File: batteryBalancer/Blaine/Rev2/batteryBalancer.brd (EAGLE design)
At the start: 101.6 x 101.6 mm, 53 parts

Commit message: Last commit of Battery balancer Rev 1
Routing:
- net KILL_SWITCH: track 211.4 -> 212.2 mm
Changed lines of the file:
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@@
 <wire x1="26.5" y1="3.175" x2="26.6855" y2="3.175" width="0.1524" layer="1"/>
 <contactref element="RLAY1" pad="CONTROL-"/>
-<contactref element="RELAY4" pad="CONTROL-"/>
 <contactref element="RELAY3" pad="CONTROL-"/>
 <contactref element="RELAY2" pad="CONTROL-"/>
@@
 <wire x1="74.2875" y1="36.8375" x2="73.66" y2="37.465" width="0.1524" layer="16"/>
 <wire x1="65.5" y1="99" x2="66.5" y2="99" width="0.1524" layer="1"/>
-<wire x1="27.432" y1="17.955" x2="25.75" y2="17.955" width="1.016" layer="1"/>
 <wire x1="27.432" y1="17.955" x2="35.9875" y2="17.955" width="1.016" layer="1"/>
 <wire x1="35.9875" y1="17.955" x2="36" y2="17.9675" width="1.016" layer="1"/>
@@
 <wire x1="69.088" y1="39.624" x2="69.85" y2="40.386" width="0.1524" layer="1"/>
 <wire x1="69.85" y1="40.386" x2="73.66" y2="40.386" width="0.1524" layer="1"/>
+<contactref element="RELAY4" pad="CONTROL-"/>
+<wire x1="25.75" y1="17.955" x2="27.432" y2="17.955" width="1.016" layer="1"/>
+<wire x1="26.6855" y1="8" x2="27.75" y2="8.25" width="0" layer="19" extent="16-16"/>
+<wire x1="26.6855" y1="7.1855" x2="26.6855" y2="8" width="0" layer="19" extent="16-16"/>
+<wire x1="26.6855" y1="3.175" x2="26.6855" y2="3.175" width="0" layer="19" extent="1-16"/>
+<wire x1="24.1455" y1="3.175" x2="26.5" y2="3.175" width="0" layer="19" extent="1-16"/>
+<wire x1="24.1455" y1="3.175" x2="24.1455" y2="3.175" width="0" layer="19" extent="1-16"/>
+<wire x1="29.2255" y1="3.175" x2="26.6855" y2="3.175" width="0" layer="19" extent="16-16"/>
+<wire x1="29.2255" y1="3.175" x2="29.2255" y2="3.175" width="0" layer="19" extent="1-16"/>
 </signal>
 <signal name="PORT_UNBALANCED">
@@
 <wire x1="91.2148" y1="11.9539125" x2="91.2148" y2="88.5352" width="0.1524" layer="1"/>
 <wire x1="25.75" y1="23.055" x2="18.2282" y2="23.055" width="1.016" layer="1"/>
-<wire x1="18.2282" y1="23.055" x2="14.1732" y2="19" width="1.016" layer="1"/>
+<wire x1="14.1732" y1="19" x2="18.2282" y2="23.055" width="1.016" layer="1"/>
 <contactref element="KILL_SWITCH" pad="1"/>
-<wire x1="14.1732" y1="18.161" x2="14.1732" y2="19" width="0" layer="19" extent="1-1"/>
+<wire x1="14.1732" y1="18.161" x2="14.1732" y2="19" width="1.016" layer="1"/>
 </signal>
 <signal name="STBD_UNFUSED">

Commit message: Touched up the battery balancer
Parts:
- removed C3, C4, C5, C6: 0.1uF, SparkFun-Capacitors:CAP-PTH-SMALL-KIT
- moved C2 20.3 mm to (65.9, 22.2), turned to 90 degrees
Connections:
- net 3.3V: now also C2.2
- net BALANCED_LOGIC: no longer C3.1
- net LOGIC_GND: now also C2.1; no longer C2.2, C3.2, C4.2, C5.2, C6.2
- net PORT_CURRENT: no longer C4.1
- net PORT_LOGIC: no longer C6.1
- net STBD_CURRENT: no longer C2.1
- net STBD_LOGIC: no longer C5.1
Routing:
- net LOGIC_GND: track 404.0 -> 386.7 mm
- net PORT_CURRENT: track 78.7 -> 68.9 mm
- net STBD_CURRENT: track 145.3 -> 139.9 mm
- net PORT_LOGIC: track 61.6 -> 56.2 mm
- net BALANCED_LOGIC: track 111.5 -> 108.2 mm
- net STBD_LOGIC: track 129.6 -> 127.2 mm
- net 3.3V: track 290.9 -> 293.2 mm
- net SDA: track 32.1 -> 33.5 mm
- net SCL: track 33.3 -> 34.6 mm
- net MOTOR_POWER1: track 57.0 -> 55.9 mm

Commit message: Fixed optoisolator values
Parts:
- R10, R11, R9: value 470 -> 10K
- R12, R13, R14: value 100 -> 2.2K
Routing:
- net GND: track 39.9 -> 32.5 mm
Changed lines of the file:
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@@
 <attribute name="OC_NEWARK" value="21H7744" x="10.541" y="56.515" size="1.778" layer="27" rot="R90" display="off"/>
 </element>
-<element name="R9" library="rcl" library_urn="urn:adsk.eagle:library:334" package="0207/7" package3d_urn="urn:adsk.eagle:package:23493/1" value="470" x="17.526" y="66.548" rot="R90"/>
-<element name="R10" library="rcl" library_urn="urn:adsk.eagle:library:334" package="0207/7" package3d_urn="urn:adsk.eagle:package:23493/1" value="470" x="75.692" y="48.514" rot="R180"/>
-<element name="R11" library="rcl" library_urn="urn:adsk.eagle:library:334" package="0207/7" package3d_urn="urn:adsk.eagle:package:23493/1" value="470" x="20.574" y="53.975" rot="R270"/>
-<element name="R12" library="rcl" library_urn="urn:adsk.eagle:library:334" package="0207/7" package3d_urn="urn:adsk.eagle:package:23493/1" value="100" x="3.048" y="64.77" rot="R90"/>
-<element name="R13" library="rcl" library_urn="urn:adsk.eagle:library:334" package="0207/7" package3d_urn="urn:adsk.eagle:package:23493/1" value="100" x="97.282" y="50.927" rot="R270"/>
-<element name="R14" library="rcl" library_urn="urn:adsk.eagle:library:334" package="0207/7" package3d_urn="urn:adsk.eagle:package:23493/1" value="100" x="3.048" y="54.61" rot="R270"/>
+<element name="R9" library="rcl" library_urn="urn:adsk.eagle:library:334" package="0207/7" package3d_urn="urn:adsk.eagle:package:23493/1" value="10K" x="17.526" y="66.548" rot="R90"/>
+<element name="R10" library="rcl" library_urn="urn:adsk.eagle:library:334" package="0207/7" package3d_urn="urn:adsk.eagle:package:23493/1" value="10K" x="75.692" y="48.514" rot="R180"/>
+<element name="R11" library="rcl" library_urn="urn:adsk.eagle:library:334" package="0207/7" package3d_urn="urn:adsk.eagle:package:23493/1" value="10K" x="20.574" y="53.975" rot="R270"/>
+<element name="R12" library="rcl" library_urn="urn:adsk.eagle:library:334" package="0207/7" package3d_urn="urn:adsk.eagle:package:23493/1" value="2.2K" x="3.048" y="64.77" rot="R90"/>
+<element name="R13" library="rcl" library_urn="urn:adsk.eagle:library:334" package="0207/7" package3d_urn="urn:adsk.eagle:package:23493/1" value="2.2K" x="97.282" y="50.927" rot="R270"/>
+<element name="R14" library="rcl" library_urn="urn:adsk.eagle:library:334" package="0207/7" package3d_urn="urn:adsk.eagle:package:23493/1" value="2.2K" x="3.048" y="54.61" rot="R270"/>
 <element name="R15" library="rcl" library_urn="urn:adsk.eagle:library:334" package="0207/7" package3d_urn="urn:adsk.eagle:package:23493/1" value="4.7K" x="20.828" y="66.548" rot="R90"/>
 <element name="R16" library="rcl" library_urn="urn:adsk.eagle:library:334" package="0207/7" package3d_urn="urn:adsk.eagle:package:23493/1" value="4.7K" x="75.692" y="51.308" rot="R180"/>
@@
 <contactref element="R11" pad="2"/>
 <contactref element="PORT_FC" pad="2"/>
-<wire x1="64.12223125" y1="85.852" x2="63.05363125" y2="86.9206" width="0.4064" layer="16"/>
-<wire x1="63.05363125" y1="86.9206" x2="62.0286" y2="86.9206" width="0.4064" layer="16"/>
-<wire x1="62.0286" y1="86.9206" x2="58.547" y2="83.439" width="0.4064" layer="16"/>
 <via x="58.547" y="83.439" extent="1-16" drill="0.35"/>
 <wire x1="58.547" y1="83.439" x2="58.547" y2="82.169" width="0.4064" layer="1"/>

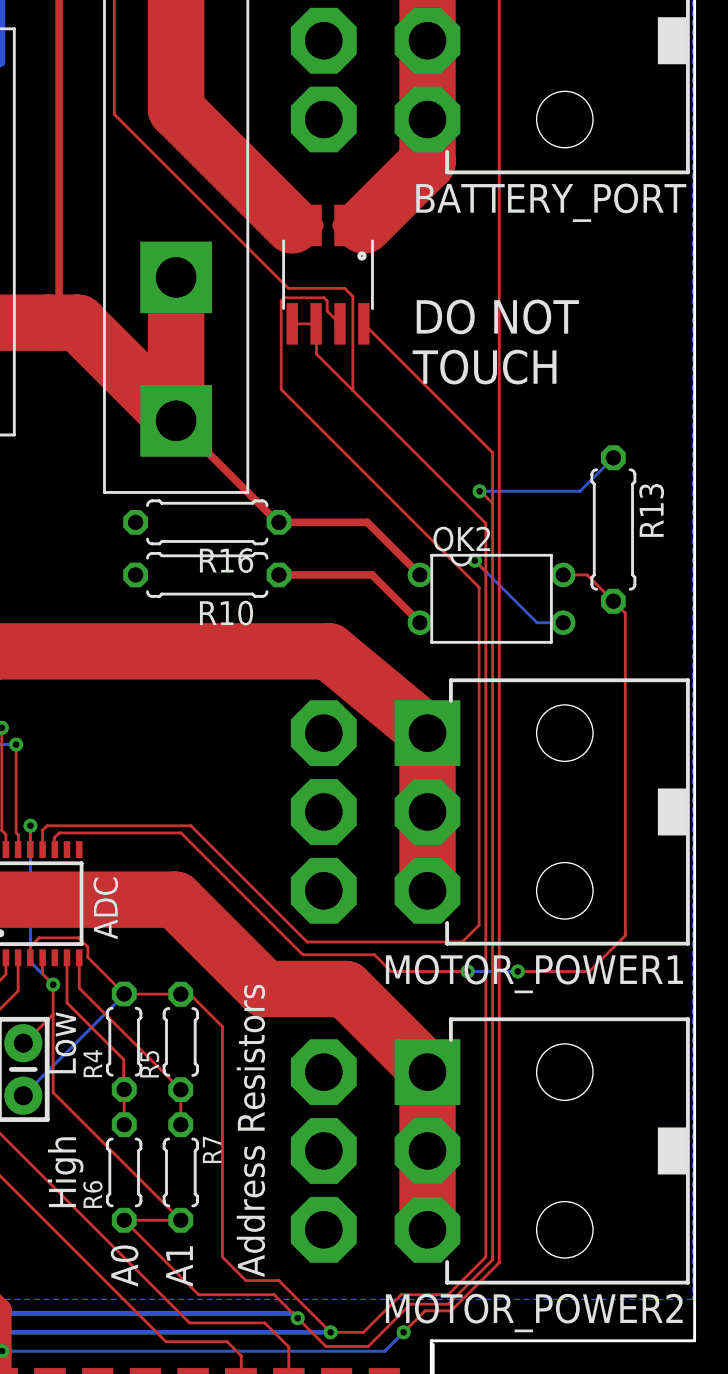
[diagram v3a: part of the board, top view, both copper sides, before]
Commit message: Updated board and added block diagram
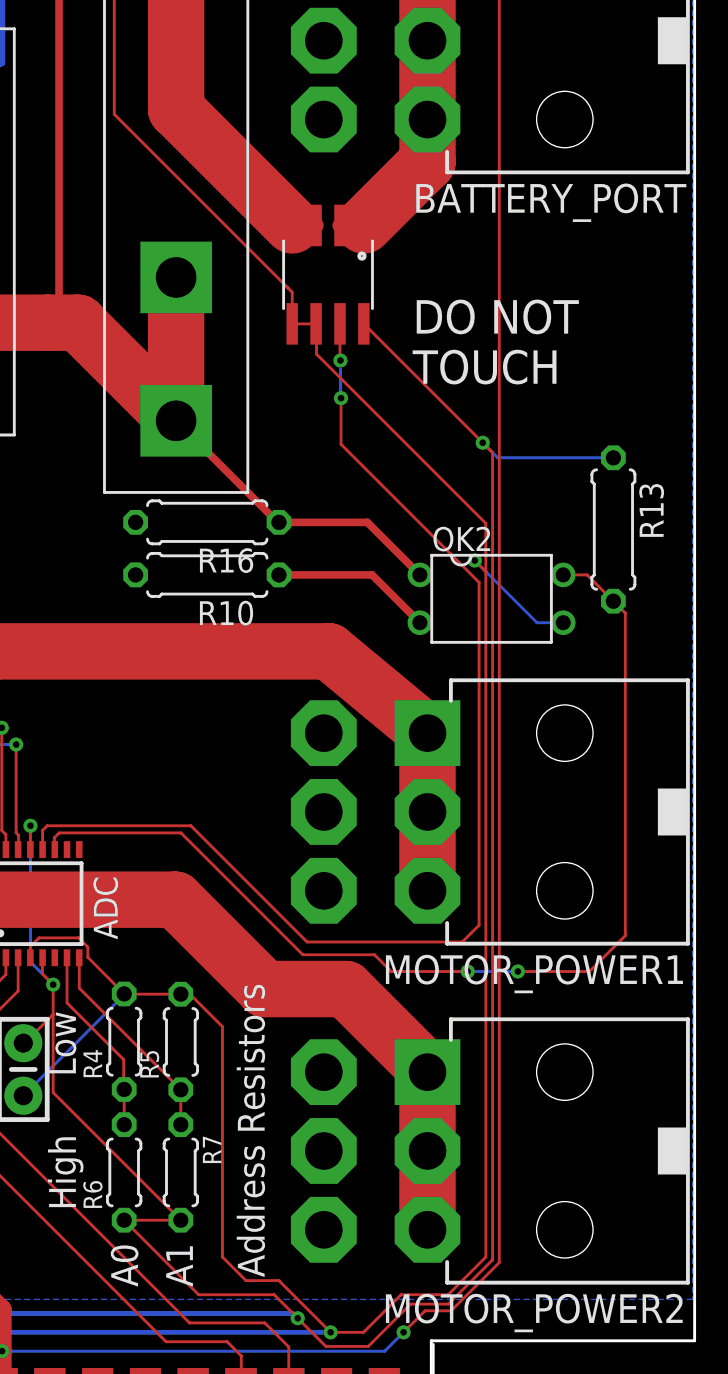
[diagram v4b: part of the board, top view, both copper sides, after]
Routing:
- net PORT_CURRENT: track 68.9 -> 62.3 mm, vias 0 -> 2
- net LOGIC_GND: track 386.7 -> 380.2 mm
- net 3.3V: track 293.2 -> 291.6 mm
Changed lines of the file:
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@@
 <layer number="27" name="tValues" color="7" fill="1" visible="yes" active="yes"/>
 <layer number="28" name="bValues" color="7" fill="1" visible="yes" active="yes"/>
-<layer number="29" name="tStop" color="7" fill="3" visible="no" active="yes"/>
-<layer number="30" name="bStop" color="7" fill="6" visible="no" active="yes"/>
-<layer number="31" name="tCream" color="7" fill="4" visible="no" active="yes"/>
-<layer number="32" name="bCream" color="7" fill="5" visible="no" active="yes"/>
-<layer number="33" name="tFinish" color="6" fill="3" visible="no" active="yes"/>
-<layer number="34" name="bFinish" color="6" fill="6" visible="no" active="yes"/>
-<layer number="35" name="tGlue" color="7" fill="4" visible="no" active="yes"/>
-<layer number="36" name="bGlue" color="7" fill="5" visible="no" active="yes"/>
-<layer number="37" name="tTest" color="7" fill="1" visible="no" active="yes"/>
-<layer number="38" name="bTest" color="7" fill="1" visible="no" active="yes"/>
+<layer number="29" name="tStop" color="7" fill="3" visible="yes" active="yes"/>
+<layer number="30" name="bStop" color="7" fill="6" visible="yes" active="yes"/>
+<layer number="31" name="tCream" color="7" fill="4" visible="yes" active="yes"/>
+<layer number="32" name="bCream" color="7" fill="5" visible="yes" active="yes"/>
+<layer number="33" name="tFinish" color="6" fill="3" visible="yes" active="yes"/>
+<layer number="34" name="bFinish" color="6" fill="6" visible="yes" active="yes"/>
+<layer number="35" name="tGlue" color="7" fill="4" visible="yes" active="yes"/>
+<layer number="36" name="bGlue" color="7" fill="5" visible="yes" active="yes"/>
+<layer number="37" name="tTest" color="7" fill="1" visible="yes" active="yes"/>
+<layer number="38" name="bTest" color="7" fill="1" visible="yes" active="yes"/>
 <layer number="39" name="tKeepout" color="4" fill="11" visible="yes" active="yes"/>
 <layer number="40" name="bKeepout" color="1" fill="11" visible="yes" active="yes"/>
@@
 <layer number="42" name="bRestrict" color="1" fill="10" visible="yes" active="yes"/>
 <layer number="43" name="vRestrict" color="2" fill="10" visible="yes" active="yes"/>
-<layer number="44" name="Drills" color="7" fill="1" visible="no" active="yes"/>
+<layer number="44" name="Drills" color="7" fill="1" visible="yes" active="yes"/>
 <layer number="45" name="Holes" color="7" fill="1" visible="yes" active="yes"/>
-<layer number="46" name="Milling" color="3" fill="1" visible="no" active="yes"/>
-<layer number="47" name="Measures" color="7" fill="1" visible="no" active="yes"/>
+<layer number="46" name="Milling" color="3" fill="1" visible="yes" active="yes"/>
+<layer number="47" name="Measures" color="7" fill="1" visible="yes" active="yes"/>
 <layer number="48" name="Document" color="7" fill="1" visible="yes" active="yes"/>
 <layer number="49" name="Reference" color="7" fill="1" visible="yes" active="yes"/>
@@
 <layer number="112" name="tSilk" color="7" fill="1" visible="yes" active="yes"/>
 <layer number="113" name="IDFDebug" color="7" fill="1" visible="yes" active="yes"/>
-<layer number="114" name="Badge_Outline" color="7" fill="1" visible="no" active="yes"/>
-<layer number="115" name="ReferenceISLANDS" color="7" fill="1" visible="no" active="yes"/>
+<layer number="114" name="Badge_Outline" color="7" fill="1" visible="yes" active="yes"/>
+<layer number="115" name="ReferenceISLANDS" color="7" fill="1" visible="yes" active="yes"/>
 <layer number="116" name="Patch_BOT" color="9" fill="4" visible="yes" active="yes"/>
 <layer number="118" name="Rect_Pads" color="7" fill="1" visible="no" active="no"/>
@@
 <wire x1="76.5" y1="24.5" x2="76.5" y2="12.25" width="0.1524" layer="1"/>
 <wire x1="76.5" y1="12.25" x2="77.75" y2="11" width="0.1524" layer="1"/>
-<wire x1="83.4315" y1="58.3185" x2="90.5" y2="51.25" width="0.1524" layer="1"/>
-<wire x1="81.5" y1="60.25" x2="83.4315" y2="58.3185" width="0.1524" layer="1"/>
+<wire x1="81.5" y1="60.25" x2="90.5" y2="51.25" width="0.1524" layer="1"/>
 <wire x1="90.5" y1="12.25" x2="90.5" y2="48.692" width="0.1524" layer="1"/>
 <wire x1="90.5" y1="48.692" x2="90.5" y2="51.25" width="0.1524" layer="1"/>
@@
 <via x="82.25" y="8.25" extent="1-16" drill="0.35"/>
 <wire x1="27.75" y1="8.25" x2="82.25" y2="8.25" width="0.254" layer="16"/>
-<wire x1="83" y1="63.75" x2="83.4315" y2="63.3185" width="0.1524" layer="1"/>
-<wire x1="83" y1="63.75" x2="80" y2="63.75" width="0.1524" layer="1"/>
 <wire x1="70.75" y1="73" x2="70.75" y2="90.75" width="0.1524" layer="1"/>
 <wire x1="70.75" y1="90.75" x2="70.25" y2="91.25" width="0.1524" layer="1"/>
 <via x="70.25" y="91.25" extent="1-16" drill="0.35"/>
 <wire x1="65.5" y1="96" x2="64.5" y2="96.75" width="0.1524" layer="16"/>
-<wire x1="80" y1="63.75" x2="70.75" y2="73" width="0.1524" layer="1"/>
+<wire x1="80" y1="63.75" x2="79.9395" y2="63.8105" width="0.1524" layer="1"/>
+<wire x1="79.9395" y1="63.8105" x2="70.75" y2="73" width="0.1524" layer="1"/>
 <wire x1="70.25" y1="91.25" x2="65.5" y2="96" width="0.1524" layer="16"/>
 <via x="64.5" y="96.75" extent="1-16" drill="0.35"/>
 <wire x1="64.5" y1="98" x2="65.5" y2="99" width="0.1524" layer="1"/>
 <wire x1="64.5" y1="98" x2="64.5" y2="96.75" width="0.1524" layer="1"/>
-<wire x1="83.4315" y1="63.3185" x2="83.4315" y2="58.3185" width="0.1524" layer="1"/>
 <contactref element="KILL_STATUS" pad="CATHODE"/>
 <contactref element="STBD_CS" pad="GND"/>
@@
 <wire x1="65.913" y1="20.828" x2="71.275" y2="26.19" width="0.1524" layer="16"/>
 <wire x1="71.275" y1="26.19" x2="71.275" y2="26.24" width="0.1524" layer="16"/>
+<wire x1="79.9395" y1="63.8105" x2="80.2075" y2="63.5425" width="0.1524" layer="1"/>
+<wire x1="80.2075" y1="63.5425" x2="80.2075" y2="61.8588" width="0.1524" layer="1"/>
 </signal>
 <signal name="PORT_UNBALANCED">
@@
 <contactref element="R6" pad="1"/>
 <contactref element="R7" pad="2"/>
-<wire x1="90.8574" y1="12.10195625" x2="90.8574" y2="52.324" width="0.1524" layer="1"/>
-<wire x1="90.8574" y1="52.324" x2="90.8574" y2="55.0189" width="0.1524" layer="1"/>
+<wire x1="90.8574" y1="12.10195625" x2="90.8574" y2="55.0189" width="0.1524" layer="1"/>
 <wire x1="79.25" y1="10.25" x2="80.5" y2="9" width="0.1524" layer="1"/>
 <wire x1="80.5" y1="9" x2="82" y2="7.5" width="0.1524" layer="1"/>
@@
 <contactref element="R12" pad="1"/>
 <contactref element="KILL_SWITCH" pad="2"/>
-<wire x1="90.8574" y1="55.0189" x2="84.0175" y2="61.8588" width="0.1524" layer="1"/>
+<wire x1="90.8574" y1="55.0189" x2="90.33715" y2="55.53915" width="0.1524" layer="1"/>
+<wire x1="90.33715" y1="55.53915" x2="84.0175" y2="61.8588" width="0.1524" layer="1"/>
 <wire x1="19.685" y1="18.161" x2="19.685" y2="9.25" width="0.4064" layer="16"/>
 <wire x1="10.25" y1="86.7087" x2="16.77" y2="93.2287" width="0.1524" layer="1"/>
@@
 <wire x1="3.048" y1="58.42" x2="6.731" y2="62.103" width="0.1524" layer="1"/>
 <wire x1="6.731" y1="62.103" x2="10.25" y2="62.103" width="0.1524" layer="1"/>
-<wire x1="90.8574" y1="52.324" x2="90.2224" y2="52.959" width="0.1524" layer="1"/>
-<wire x1="90.2224" y1="52.959" x2="90.17" y2="52.959" width="0.1524" layer="1"/>
-<via x="90.17" y="52.959" extent="1-16" drill="0.35"/>
-<wire x1="90.17" y1="52.959" x2="95.504" y2="52.959" width="0.1524" layer="16"/>
-<wire x1="95.504" y1="52.959" x2="97.282" y2="54.737" width="0.1524" layer="16"/>
 <contactref element="ADC" pad="IN3"/>
 <wire x1="66.2875" y1="33.9125" x2="66.2875" y2="35.1725" width="0.1524" layer="1"/>
@@
 <wire x1="65.913" y1="23.622" x2="65.976" y2="23.622" width="0.1524" layer="1"/>
 <wire x1="65.976" y1="23.622" x2="67.5" y2="25.146" width="0.1524" layer="1"/>
+<wire x1="97.282" y1="54.737" x2="91.1393" y2="54.737" width="0.1524" layer="16"/>
+<wire x1="91.1393" y1="54.737" x2="90.33715" y2="55.53915" width="0.1524" layer="16"/>
+<via x="90.33715" y="55.53915" extent="1-16" drill="0.35"/>
 </signal>
 <signal name="ADC_A0">
@@
 <signal name="PORT_CURRENT">
 <contactref element="PORT_CS" pad="VIOUT"/>
-<wire x1="82.0635" y1="63.080175" x2="81.898775" y2="63.2449" width="0.1524" layer="1"/>
-<wire x1="79.786225" y1="63.2449" x2="79.6215" y2="63.080175" width="0.1524" layer="1"/>
-<wire x1="81.898775" y1="63.2449" x2="79.786225" y2="63.2449" width="0.1524" layer="1"/>
-<wire x1="82.7475" y1="61.8588" x2="82.0635" y2="62.5428" width="0.1524" layer="1"/>
-<wire x1="82.0635" y1="62.5428" x2="82.0635" y2="63.080175" width="0.1524" layer="1"/>
-<wire x1="79.6215" y1="63.080175" x2="79.6215" y2="58.3785" width="0.1524" layer="1"/>
-<wire x1="79.6215" y1="58.3785" x2="90.1426" y2="47.8574" width="0.1524" layer="1"/>
-<wire x1="90.1426" y1="47.8574" x2="90.1426" y2="29.8926" width="0.1524" layer="1"/>
+<wire x1="90.1426" y1="48.1168625" x2="90.1426" y2="29.8926" width="0.1524" layer="1"/>
 <wire x1="90.1426" y1="29.8926" x2="89.25" y2="29" width="0.1524" layer="1"/>
 <wire x1="81" y1="29" x2="89.25" y2="29" width="0.1524" layer="1"/>
@@
 <wire x1="67.183" y1="35.179" x2="74.821" y2="35.179" width="0.1524" layer="1"/>
 <wire x1="74.821" y1="35.179" x2="81" y2="29" width="0.1524" layer="1"/>
+<via x="82.7721" y="59.9104375" extent="1-16" drill="0.35"/>
+<wire x1="82.7721" y1="59.9104375" x2="82.7475" y2="59.9350375" width="0.1524" layer="1"/>
+<wire x1="82.7475" y1="59.9350375" x2="82.7475" y2="61.8588" width="0.1524" layer="1"/>
+<wire x1="82.7721" y1="59.9104375" x2="82.7721" y2="57.9439" width="0.1524" layer="16"/>
+<wire x1="82.7721" y1="57.9439" x2="82.804" y2="57.912" width="0.1524" layer="16"/>
+<via x="82.804" y="57.912" extent="1-16" drill="0.35"/>
+<wire x1="82.804" y1="57.912" x2="82.804" y2="55.4554625" width="0.1524" layer="1"/>
+<wire x1="82.804" y1="55.4554625" x2="90.1426" y2="48.1168625" width="0.1524" layer="1"/>
 </signal>
 <signal name="STBD_CURRENT">

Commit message: Finished it up and made the gerber files
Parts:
- added C3: (no value), rcl:E2-4
- turned C2 to 270 degrees
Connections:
- net 3.3V: now also ADC.VREF, C2.1, C3.+; no longer ADC.IN3, C2.2
- net LOGIC_GND: now also C2.2, C3.-; no longer C2.1
- net PORT_CURRENT: now also ADC.IN3; no longer ADC.IN4
- net PORT_LOGIC: now also ADC.IN4; no longer ADC.IN5
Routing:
- net LOGIC_GND: track 380.2 -> 385.3 mm
- net 3.3V: track 291.6 -> 289.5 mm
- net SDA: track 33.5 -> 34.7 mm
- net SCL: track 34.6 -> 35.4 mm
- net PORT_CURRENT: track 62.3 -> 62.9 mm
- net PORT_LOGIC: track 56.2 -> 56.9 mm
